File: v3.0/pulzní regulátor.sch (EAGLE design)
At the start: 19 parts, among them Q1 NX3008, Q2 NX3008, Q3 NX3008, Q4 NX3008

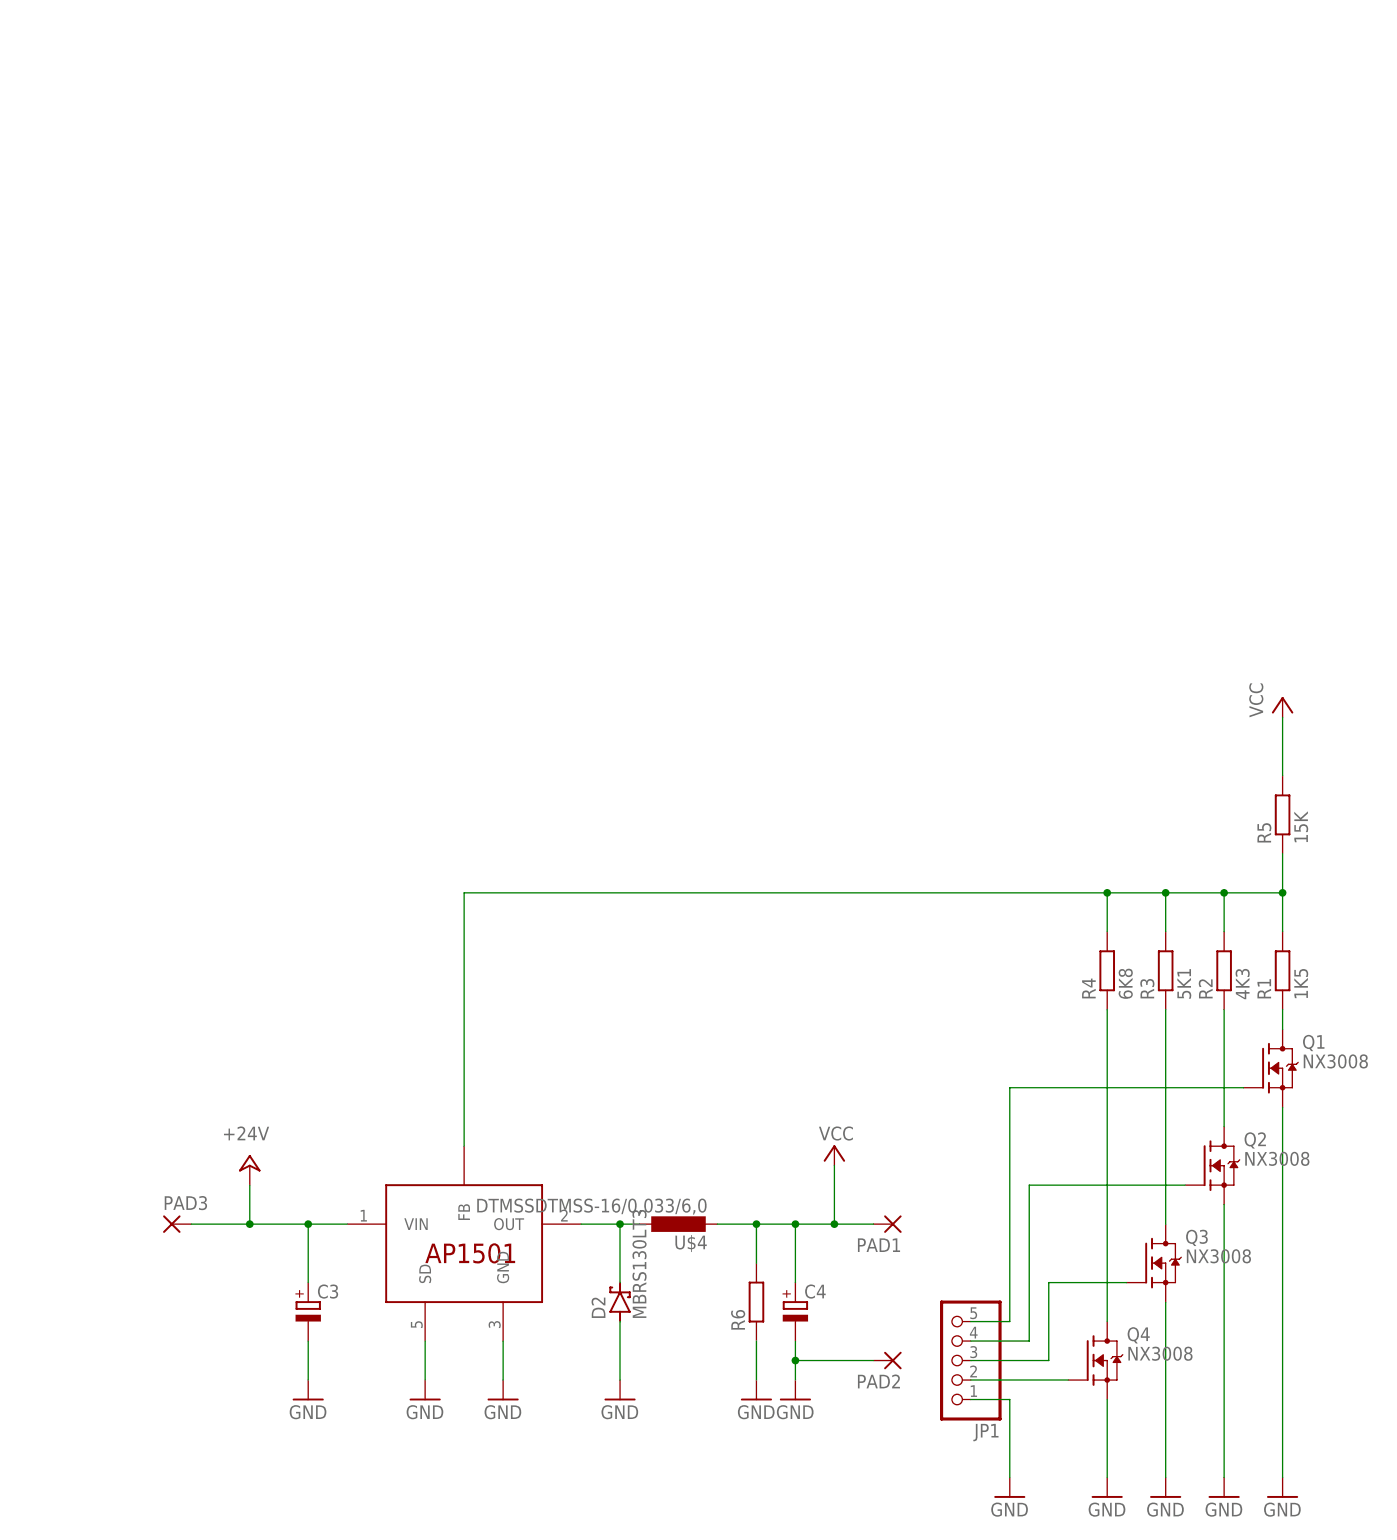
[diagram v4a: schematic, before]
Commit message: zpřehledněno schéma spínaného zdroje a dokončena jeho dokumentace
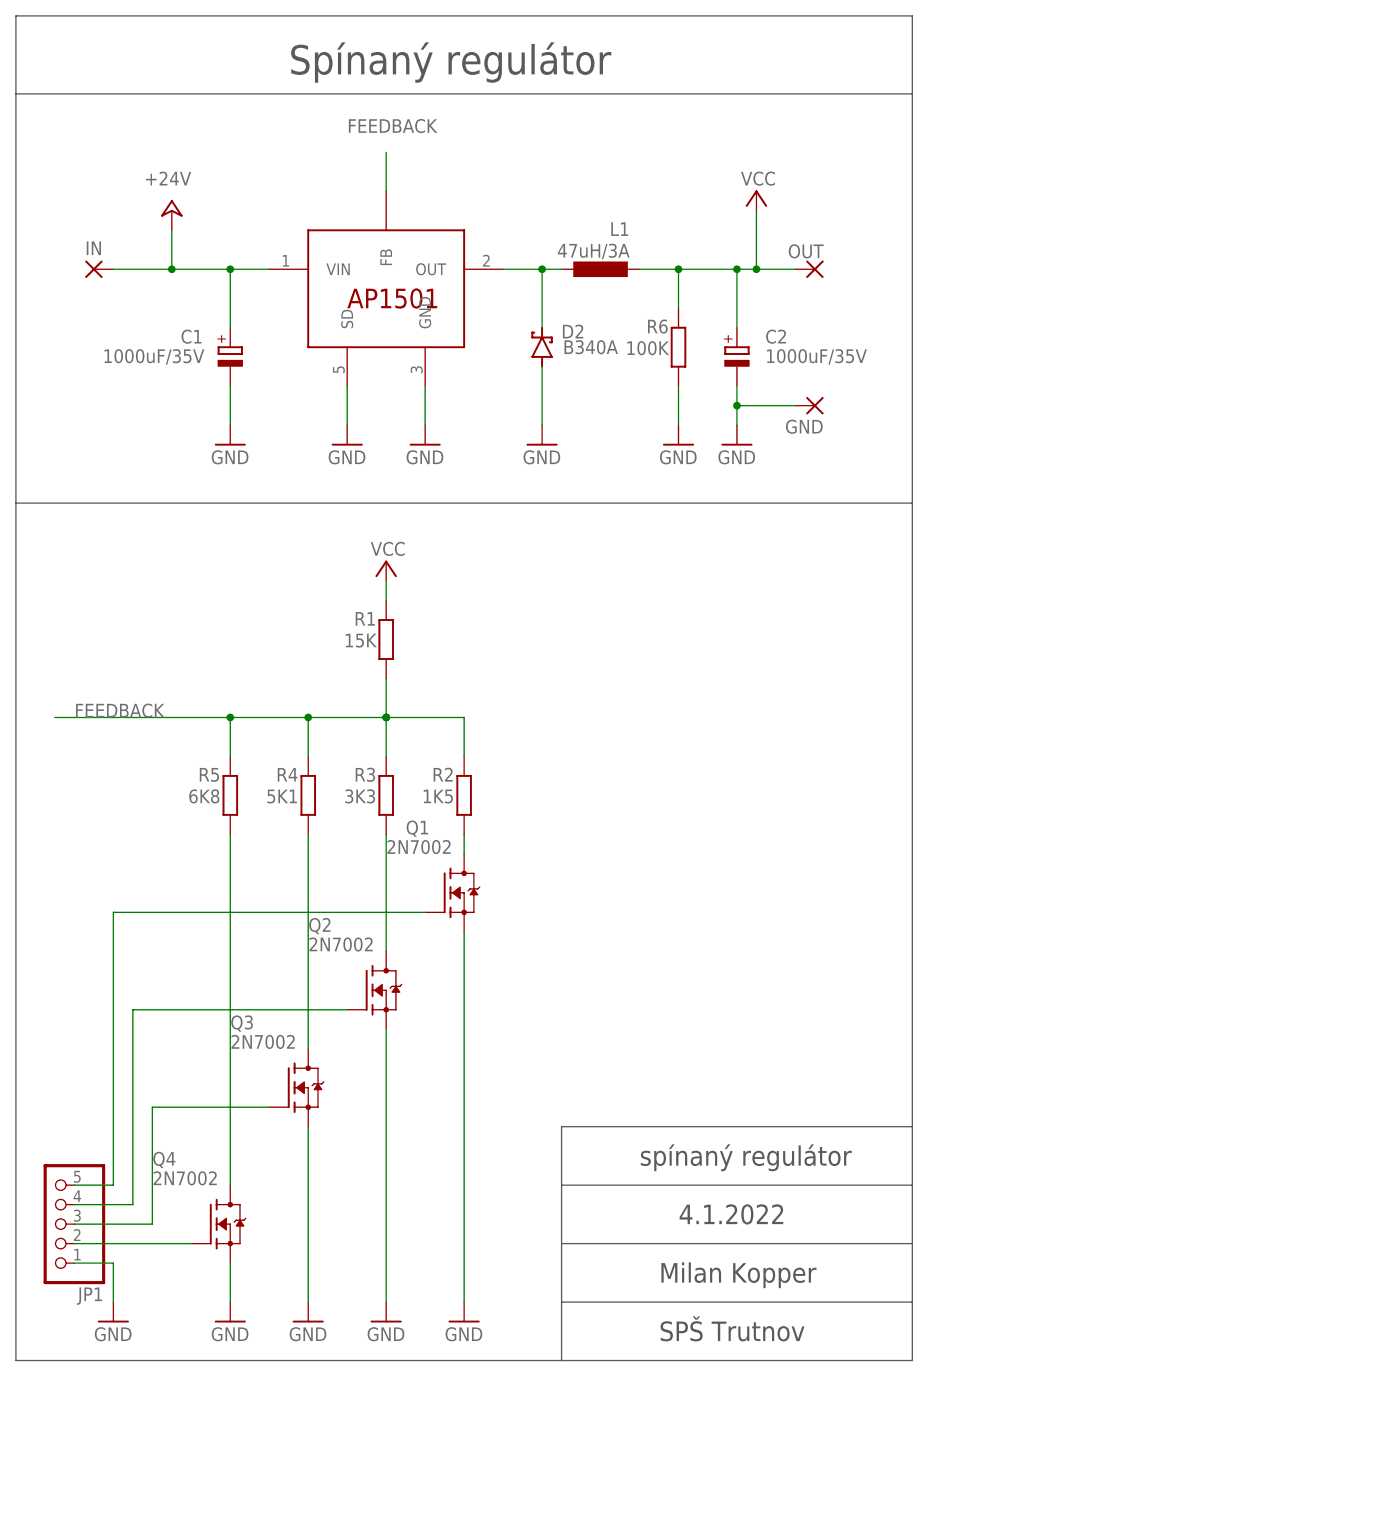
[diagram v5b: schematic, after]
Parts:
- removed C3, C4: (no value), rcl:CPOL-EUE5-10.5
- removed PAD1, PAD2, PAD3: (no value), wirepad:3,17/1,3
- removed U$4: DTMSSDTMSS-16/0,033/6,0, induktory a trafa:DTMSSDTMSS-16/0,033/6,0
- added C1, C2: 1000uF/35V, rcl:CPOL-EUE5-10.5
- added GND, IN, OUT: (no value), wirepad:3,17/1,3
- added L1: 47uH/3A, induktory a trafa:DTMSSDTMSS-16/0,033/6,0
- D2: value MBRS130LT3 -> B340A
- Q1, Q2, Q3, Q4: value NX3008 -> 2N7002
- R1: value 1K5 -> 15K
- R2: value 4K3 -> 1K5
- R3: value 5K1 -> 3K3
- R4: value 6K8 -> 5K1
- R5: value 15K -> 6K8
- R6: value (none) -> 100K
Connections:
- removed net N$6: R1.2, R2.2, R3.2, R4.2, R5.1, U$2.FB
- new net FEEDBACK: R1.1, R2.2, R3.2, R4.2, R5.2, U$2.FB
- net +24V: now also C1.+, IN.P; no longer C3.+, PAD3.P
- net GND: now also C1.-, C2.-, GND.P; no longer C3.-, C4.-, PAD2.P
- net N$1: now also R5.1; no longer R4.1
- net N$11: now also R3.1; no longer R2.1
- net N$12: now also R4.1; no longer R3.1
- net N$3: now also L1.1; no longer U$4.1
- net N$7: now also R2.1; no longer R1.1
- net VCC: now also C2.+, L1.2, OUT.P, R1.2; no longer C4.+, PAD1.P, R5.2, U$4.2
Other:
- note added: "4.1.2022"
- note added: "Milan Kopper"
- note added: "SPŠ Trutnov"
- note added: "Spínaný regulátor"
- note added: "spínaný regulátor"
- moved on the sheet: D2, JP1, Q1, Q2, Q3, Q4, R1, R2, R3, R4, R5, R6

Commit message: přidání 3D modelu úpravy dokumentace
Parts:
- R1, R2, R3, R4, R5: device rcl_my:R-EU_M0805 -> rcl:R-EU_R0805
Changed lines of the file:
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@@
 </classes>
 <parts>
-<part name="U$2" library="regulators" deviceset="AP1501" device="TO220"/>
+<part name="U$2" library="regulators" deviceset="AP1501" device="TO220" override_package3d_urn="urn:adsk.eagle:package:33936918/2" override_package_urn="urn:adsk.eagle:footprint:4814/1"/>
 <part name="L1" library="induktory a trafa" deviceset="DTMSS" device="DTMSS-16/0,033/6,0" package3d_urn="urn:adsk.eagle:package:24991841/2" value="47uH/3A"/>
 <part name="GND1" library="supply1" library_urn="urn:adsk.eagle:library:371" deviceset="GND" device=""/>
@@
 <part name="D2" library="diode" library_urn="urn:adsk.eagle:library:210" deviceset="MBRS130LT3" device="" package3d_urn="urn:adsk.eagle:package:43404/2" value="B340A"/>
 <part name="GND10" library="supply1" library_urn="urn:adsk.eagle:library:371" deviceset="GND" device=""/>
-<part name="Q1" library="NEXPERIA " deviceset="NX3008" device="" value="2N7002"/>
-<part name="Q2" library="NEXPERIA " deviceset="NX3008" device="" value="2N7002"/>
-<part name="Q3" library="NEXPERIA " deviceset="NX3008" device="" value="2N7002"/>
-<part name="Q4" library="NEXPERIA " deviceset="NX3008" device="" value="2N7002"/>
+<part name="Q1" library="NEXPERIA " deviceset="NX3008" device="" override_package3d_urn="urn:adsk.eagle:package:33936901/2" override_package_urn="urn:adsk.eagle:footprint:33936902/1" value="2N7002"/>
+<part name="Q2" library="NEXPERIA " deviceset="NX3008" device="" override_package3d_urn="urn:adsk.eagle:package:33936871/2" override_package_urn="urn:adsk.eagle:footprint:33936872/1" value="2N7002"/>
+<part name="Q3" library="NEXPERIA " deviceset="NX3008" device="" override_package3d_urn="urn:adsk.eagle:package:33936865/2" override_package_urn="urn:adsk.eagle:footprint:33936866/1" value="2N7002"/>
+<part name="Q4" library="NEXPERIA " deviceset="NX3008" device="" override_package3d_urn="urn:adsk.eagle:package:33936903/2" override_package_urn="urn:adsk.eagle:footprint:33936905/1" value="2N7002"/>
 <part name="JP1" library="pinhead" library_urn="urn:adsk.eagle:library:325" deviceset="PINHD-1X5" device="" package3d_urn="urn:adsk.eagle:package:22469/2"/>
 <part name="GND11" library="supply1" library_urn="urn:adsk.eagle:library:371" deviceset="GND" device=""/>
@@
 <part name="GND14" library="supply1" library_urn="urn:adsk.eagle:library:371" deviceset="GND" device=""/>
 <part name="GND15" library="supply1" library_urn="urn:adsk.eagle:library:371" deviceset="GND" device=""/>
-<part name="R2" library="rcl_my" deviceset="R-EU_" device="M0805" value="1K5"/>
-<part name="R3" library="rcl_my" deviceset="R-EU_" device="M0805" value="3K3"/>
-<part name="R4" library="rcl_my" deviceset="R-EU_" device="M0805" value="5K1"/>
-<part name="R5" library="rcl_my" deviceset="R-EU_" device="M0805" value="6K8"/>
-<part name="R1" library="rcl_my" deviceset="R-EU_" device="M0805" value="15K"/>
+<part name="R2" library="rcl" library_urn="urn:adsk.eagle:library:334" deviceset="R-EU_" device="R0805" package3d_urn="urn:adsk.eagle:package:23553/2" value="1K5"/>
+<part name="R3" library="rcl" library_urn="urn:adsk.eagle:library:334" deviceset="R-EU_" device="R0805" package3d_urn="urn:adsk.eagle:package:23553/2" value="3K3"/>
+<part name="R4" library="rcl" library_urn="urn:adsk.eagle:library:334" deviceset="R-EU_" device="R0805" package3d_urn="urn:adsk.eagle:package:23553/2" value="5K1"/>
+<part name="R5" library="rcl" library_urn="urn:adsk.eagle:library:334" deviceset="R-EU_" device="R0805" package3d_urn="urn:adsk.eagle:package:23553/2" value="6K8"/>
+<part name="R1" library="rcl" library_urn="urn:adsk.eagle:library:334" deviceset="R-EU_" device="R0805" package3d_urn="urn:adsk.eagle:package:23553/2" value="15K"/>
 <part name="P+2" library="supply1" library_urn="urn:adsk.eagle:library:371" deviceset="VCC" device=""/>
 <part name="P+3" library="supply1" library_urn="urn:adsk.eagle:library:371" deviceset="VCC" device=""/>
-<part name="OUT" library="wirepad" library_urn="urn:adsk.eagle:library:412" deviceset="3,17/1,3" device="" package3d_urn="urn:adsk.eagle:package:30833/1"/>
-<part name="GND" library="wirepad" library_urn="urn:adsk.eagle:library:412" deviceset="3,17/1,3" device="" package3d_urn="urn:adsk.eagle:package:30833/1"/>
-<part name="IN" library="wirepad" library_urn="urn:adsk.eagle:library:412" deviceset="3,17/1,3" device="" package3d_urn="urn:adsk.eagle:package:30833/1"/>
+<part name="OUT" library="wirepad" library_urn="urn:adsk.eagle:library:412" deviceset="3,17/1,3" device="" package3d_urn="urn:adsk.eagle:package:30833/1" override_package3d_urn="urn:adsk.eagle:package:33936895/2" override_package_urn="urn:adsk.eagle:footprint:30815/1"/>
+<part name="GND" library="wirepad" library_urn="urn:adsk.eagle:library:412" deviceset="3,17/1,3" device="" package3d_urn="urn:adsk.eagle:package:30833/1" override_package3d_urn="urn:adsk.eagle:package:33936879/2" override_package_urn="urn:adsk.eagle:footprint:30815/1"/>
+<part name="IN" library="wirepad" library_urn="urn:adsk.eagle:library:412" deviceset="3,17/1,3" device="" package3d_urn="urn:adsk.eagle:package:30833/1" override_package3d_urn="urn:adsk.eagle:package:33936877/2" override_package_urn="urn:adsk.eagle:footprint:30815/1"/>
 <part name="R6" library="rcl" library_urn="urn:adsk.eagle:library:334" deviceset="R-EU_" device="R0805" package3d_urn="urn:adsk.eagle:package:23553/2" value="100K"/>
 <part name="GND3" library="supply1" library_urn="urn:adsk.eagle:library:371" deviceset="GND" device=""/>
@@
 packages will not be understood (or retained) with this version.
 </note>
+<note version="9.4" severity="warning">
+Since Version 9.4, EAGLE supports the overriding of 3D packages
+in schematics and board files. Those overridden 3d packages
+will not be understood (or retained) with this version.
+</note>
 <note version="8.4" severity="warning">
